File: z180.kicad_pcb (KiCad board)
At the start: 2 copper layers, 89.7 x 64.8 mm, 69 parts, among them J1 SERIAL_IO, J2 USB_POWER, J3 zdbus, J4 zabus, J5 zcbus, J6 USB_DATA, J7 POWER_IN, J8 Conn_01x08, J9 MEM_ADDR, SW1 SW_Push, U1 74LS138, U2 28C256, U3 AS6C1008-55PCN, U4 74LS138, U5 DS1813, U8 74LS05, Y1 Crystal

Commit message: layout mostly complete
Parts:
- removed C14, C17, C7, C8: 0.1µF, Capacitor_SMD:C_1206_3216Metric_Pad1.42x1.75mm_HandSolder
- removed D1, D2, D4, D5, D6, D7: LED, LED_SMD:LED_1206_3216Metric_Pad1.42x1.75mm_HandSolder
- removed J5: zcbus, Connector_IDC:IDC-Header_2x08_P2.54mm_Vertical
- removed R5, R6, R7, R8: 300, Resistor_SMD:R_1206_3216Metric_Pad1.42x1.75mm_HandSolder
- removed TP5: TST_WAIT, TestPoint:TestPoint_THTPad_1.0x1.0mm_Drill0.5mm
- removed TP6: TST_HALT, TestPoint:TestPoint_THTPad_1.0x1.0mm_Drill0.5mm
- removed U8: 74LS05, Package_SO:SOIC-14_3.9x8.7mm_P1.27mm
- added J10: BUSCTRL, Connector_PinHeader_2.54mm:PinHeader_2x04_P2.54mm_Vertical, F.Cu at (48.3, 141.0)
- added JP1: SolderJumper_2_Bridged, NetTie:NetTie-2_SMD_Pad0.5mm, F.Cu at (66.0, 152.4)
- added JP2: SolderJumper_2_Bridged, NetTie:NetTie-2_SMD_Pad0.5mm, B.Cu at (72.1, 152.4)
- added MH3: MountingHole_Pad, MountingHole:MountingHole_2.2mm_M2_Pad_Via, F.Cu at (48.3, 104.1)
- added MH4: MountingHole_Pad, MountingHole:MountingHole_2.2mm_M2_Pad_Via, F.Cu at (127.0, 104.1)
- C20: value C_Small -> 0.1µF; moved to F.Cu
- J3: footprint Connector_IDC:IDC-Header_2x08_P2.54mm_Vertical -> Connector_PinHeader_2.54mm:PinHeader_2x08_P2.54mm_Vertical
- J4: value zabus -> STATUS; footprint Connector_IDC:IDC-Header_2x08_P2.54mm_Vertical -> Connector_PinHeader_2.54mm:PinHeader_1x03_P2.54mm_Vertical
- J9: footprint Connector_PinHeader_1.27mm:PinHeader_1x06_P1.27mm_Vertical -> Connector_PinHeader_2.54mm:PinHeader_1x06_P2.54mm_Vertical
- MH2: footprint MountingHole:MountingHole_2.2mm_M2_Pad_Via -> MountingHole:MountingHole_2.2mm_M2
- R1, R3: moved to F.Cu
- R2: value 300 -> 10k
- R4: value 300 -> 22R
- U2: footprint Package_DIP:DIP-28_W15.24mm_Socket -> z180:DIP-28_Piggyback_Memory_W15.24mm_Socket
- moved J6 88.7 mm to (123.4, 149.2), turned to 270 degrees
- moved J2 87.9 mm to (123.2, 143.0), turned to 90 degrees
- moved C9 84.4 mm to (126.0, 128.5), turned to 0 degrees
- moved D3 81.3 mm to (120.9, 131.6), turned to 0 degrees
- moved R3 81.2 mm to (120.9, 134.1), turned to 0 degrees
- moved J7 80.7 mm to (125.2, 134.4), turned to 90 degrees
- moved C11 71.7 mm to (113.5, 150.4), turned to 0 degrees
- moved F1 68.5 mm to (113.8, 133.9), turned to 90 degrees
- moved C10 64.7 mm to (113.5, 140.7), turned to 0 degrees
- moved R2 52.4 mm to (85.3, 141.2), turned to 0 degrees
- moved J4 44.1 mm to (50.8, 116.8), turned to 0 degrees
- moved MH1 43.1 mm to (127.0, 152.4)
- moved C19 40.7 mm to (67.8, 152.4), turned to 0 degrees
- moved U5 34.1 mm to (72.0, 147.9), turned to 0 degrees
- moved R1 33.8 mm to (68.1, 147.8), turned to 270 degrees
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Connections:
- net Net-(R10-Pad2) renamed /G1
- net Net-(R11-Pad1) renamed /~G2B
- net Net-(R9-Pad2) renamed /CE2
- C10 pad 1: /PWRIN_5V -> /REG_5V
- C10 pad 2: Earth -> /PWRIN_GND
- C11 pad 1: /PWRIN_5V -> /REG_5V
- C11 pad 2: Earth -> /PWRIN_GND
- C19 pad 1: +5V -> /REG_5V
- C19 pad 2: Earth -> /PWRIN_GND
- C9 pad 1: +5V -> /IO_5V
- D3 pad 2: +5V -> /REG_5V
- F1 pad 1: +5V -> /REG_5V
- J3 pad 10: /D5 -> /D2
- J3 pad 11: /D4 -> /D6
- J3 pad 12: /D3 -> /D7
- J3 pad 13: /D2 -> /D4
- J3 pad 14: /D1 -> /D5
- J3 pad 16: /D0 -> /D3
- J3 pad 2: +5V -> /IO_5V
- J3 pad 3: /~RD -> /A2
- J3 pad 4: /~WR -> /A1
- J3 pad 6: /A1 -> /~WR
- J3 pad 7: /A2 -> /~RD
- J3 pad 8: /D7 -> /D0
- J3 pad 9: /D6 -> /D1
- J4 pad 1: Earth -> /~HALT
- J4 pad 2: +5V -> /~M1
- J4 pad 3: /A3 -> /ST
- J7 pad 4: Earth -> /PWRIN_GND
- MH1 pad 1: Earth -> /PWRIN_GND
- R2 pad 2: Net-(D1-Pad2) -> /~EEWR
- R3 pad 2: Earth -> /PWRIN_GND
- R4 pad 1: +5V -> /REG_5V
- R4 pad 2: Net-(D2-Pad2) -> /IO_5V
- U2 pad 27: Net-(U2-Pad27) -> /~EEWR
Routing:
- net Earth: track 203.7 -> 84.5 mm, vias 26 -> 33
- net /~BUSACK: track 115.8 -> 11.7 mm, vias 2 -> 0
- net /~MREQ: track 135.5 -> 32.0 mm, vias 1 -> 0
- net +5V: track 328.3 -> 231.9 mm, vias 5 -> 4
- net /~M1: track 99.8 -> 7.54 mm, vias 1 -> 0
- net /REG_5V: track 0.00 -> 92.0 mm
- net /PWRIN_GND: track 0.00 -> 84.1 mm
- net /~RESET: track 118.9 -> 37.9 mm, vias 2 -> 1
- net /A13: track 74.2 -> 13.4 mm
- net /D2: track 111.1 -> 51.3 mm, vias 1 -> 0
- net /A10: track 80.7 -> 23.2 mm
- net /D0: track 107.0 -> 50.6 mm, vias 1 -> 0
- net /A7: track 120.7 -> 66.4 mm
- net /A12: track 78.6 -> 26.8 mm, vias 1 -> 0
- net /D1: track 107.4 -> 57.3 mm, vias 1 -> 0
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- added copper zone on B.Cu, net /PWRIN_GND
- added copper zone on F.Cu, net /PWRIN_GND
- removed copper zone on F.Cu, net +5V
- removed copper zone on F.Cu, net /USB_Vbus
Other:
- board size 89.7 x 64.8 mm -> 83.8 x 53.3 mm
- board text added: "+"
- board text added: "-"
- board text added: "1"
- board text added: "5V A1 ~WR~ D0 D2 D7 D5 D3"
- board text added: "A10 A8 A6 A4 A3 A1 ST ~INT1~ ~NMI~"
- board text added: "A9 A7 A5 GND A2 A0 ~INT2~ ~INT0~"
- board text added: "Ax2 Ax3 Ax4 Ax5 Ax6 Ax7"
- board text added: "D3 D4 D5 D6 D7 ~CE A10 ~RD A11 A9 A8 A13 ~WR CE2 A15 +5V"
- board text added: "D7 D6 D4 D5 D2 D3 D0 D1 A19 GND A18 +5V A16 A17 A14 A15 A12 A13 A11"
- board text added: "GND A2 A0 ~RD~ D1 D6 D4 ~IORQ~"
- board text added: "GND D2 D1 D0 A0 A1 A2 A3 A4 A5 A6 A7 A12 A14 A16 NC"
- board text added: "I/O"
- board text added: "I/O Address Decoder"
- board text added: "Mem Address Decoder"
- board text added: "Piggyback ROM"
- board text added: "Power"
- board text added: "ROM/RAM"
- board text added: "RXS CKS RXA1 ~RTS0~ RXA0 ~DCD0~"
- board text added: "Reset"
- board text added: "Serial I/O"
- board text added: "TXS TXA1 CKA1 ~CTS0~ TXA0 CKA0"
- board text added: "USB data"
- board text added: "Z8S180 CPU"
- board text added: "~CTS0~ TXA0 CKA0 NC ~CKA1~ RXS ~DREQ1~ ~HALT~"
- board text added: "~INT0~ ~NMI~ ~BsReq~ ~WAIT~"
- board text added: "~INT2~ ~INT1~ ~RESET~ ~BsAck~"
- board text added: "~IORQ6~ ~IORQ4~ ~IORQ2~ ~IORQ0~"
- board text added: "~IORQ7~ ~IORQ5~ ~IORQ3~ ~IORQ1~"
- board text added: "~IORQx~ (I/O Select) Addr 0x80+8x"
- board text added: "~IORQ~ ~RFSH~ E ~MREQ~ ~WR~ ~M1~ PHI ~RD~ GND GND EXTAL XTAL ~BUSACK~ ~WAIT~ ~RESET~ ~BUSREQ~"
- board text added: "~RTS0~ ~DCD0~ RXA0 TXA1 RXA1 TXS CKS TEND1"
- board text removed: "7 6 5 4 3 2"
- board text removed: "A13 A11 A9 A7 A5 A3 GND"
- board text removed: "A14 A15 A12 A10 A8 A6 A4 5V"
- board text removed: "BUS"
- board text removed: "CKS TXA1"
- board text removed: "D0 D1 D3 D5 D7 A1 ~WR~ 5V"
- board text removed: "POWER"
- board text removed: "RX"
- board text removed: "RXA0 TXA0"
- board text removed: "RXA1 CKA1"
- board text removed: "RXS TXS"
- board text removed: "ST"
- board text removed: "TX"
- board text removed: "~BUS ACK"
- board text removed: "~BUS REQ"
- board text removed: "~DCD0 CKA0"
- board text removed: "~HALT"
- board text removed: "~INT0"
- board text removed: "~INT1"
- board text removed: "~INT2"
- board text removed: "~IORQ~ D2 D4 D6 A2 A0 ~RD~ GND"
- board text removed: "~M1"
- board text removed: "~MREQ"
- board text removed: "~NMI"
- board text removed: "~RST"
- board text removed: "~RTS0 ~CTS0"
- board text removed: "~WAIT"

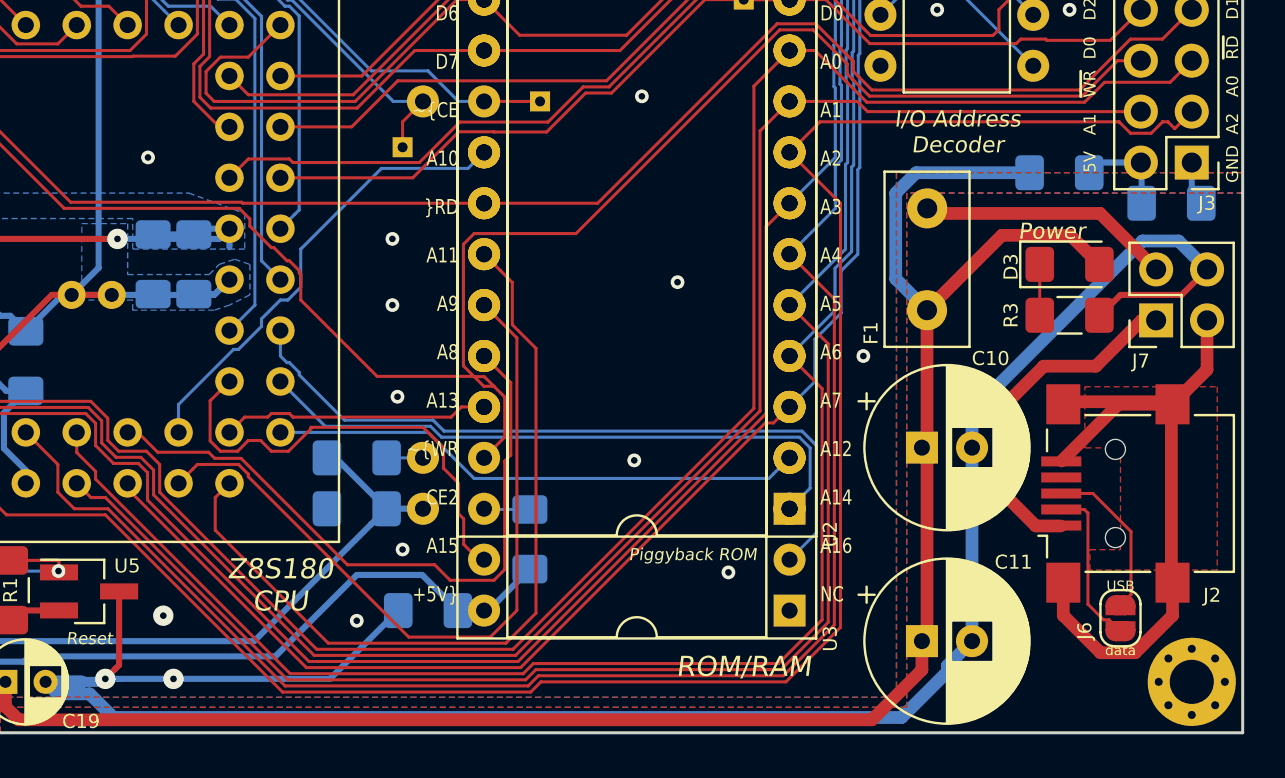
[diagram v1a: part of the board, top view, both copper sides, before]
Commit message: add logo
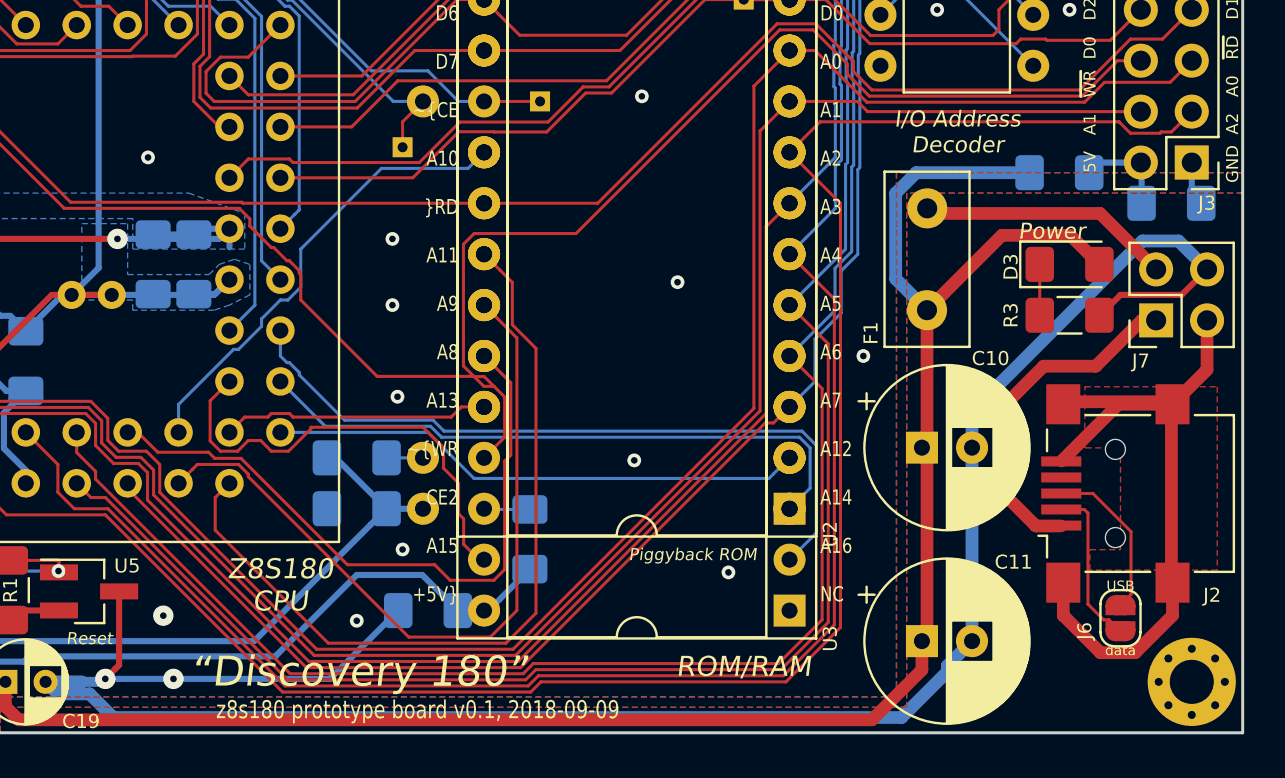
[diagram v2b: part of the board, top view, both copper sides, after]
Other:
- board text added: "USB power in"
- board text added: "i/o power"
- board text added: "power in"
- board text added: "z8s180 prototype board v0.1, 2018-09-09"
- board text added: "“Discovery 180”"

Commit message: final for v0.1
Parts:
- removed R1: [1k], Resistor_SMD:R_1206_3216Metric_Pad1.42x1.75mm_HandSolder
- added RN1: 10k x4, Resistor_SMD:R_Array_Convex_4x1206, B.Cu at (56.4, 51.8)
- added RN2: 10k x4, Resistor_SMD:R_Array_Convex_4x1206, B.Cu at (59.3, 63.0)
- added bird1: bird_logo, z180:bird, F.Cu at (70.6, 67.1)
- added bird1: SYM_Flash_Small, z180:bird, B.Cu at (97.3, 66.8)
- added discovery1: discovery_logo, z180:discovery, B.Cu at (78.5, 68.6)
- added discovery1: SYM_Flash_Small, z180:discovery, F.Cu at (89.2, 68.6)
- added oshw1: Logo_Open_Hardware_Small, Symbol:OSHW-Symbol_6.7x6mm_SilkScreen, B.Cu at (114.3, 65.5)
- F1: value 500mA -> 650mA
- J2: value USB_POWER -> USB Micro-B 105017; footprint Connector_USB:USB_Mini-B_Lumberg_2486_01_Horizontal -> Connector_USB:USB_Micro-B_Molex-105017-0001
- MH1, MH2, MH3, MH4: value MountingHole_Pad -> M2
- R3: value 330 -> 330R
- U1, U4: value 74LS138 -> 74HCT138
- moved J6 90.8 mm to (115.3, 58.8)
- moved C13 84.1 mm to (55.1, 46.0)
- moved CPU1 84.1 mm to (49.5, 46.0)
- moved J7 84.1 mm to (118.6, 50.5)
- moved TP1 84.1 mm to (54.1, 48.3)
- moved C10 84.1 mm to (106.9, 56.9)
- moved C15 84.1 mm to (97.0, 24.9)
- moved C19 84.1 mm to (61.2, 68.6)
- moved C6 84.1 mm to (78.7, 59.9)
- moved F1 84.1 mm to (107.2, 50.0)
- moved J3 84.1 mm to (120.4, 42.7)
- moved JP1 84.1 mm to (59.4, 68.6)
- moved JP2 84.1 mm to (65.5, 68.6)
- moved MH1 84.1 mm to (120.4, 68.6)
- moved MH2 84.1 mm to (41.7, 68.6)
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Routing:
- net +5V: track 231.9 -> 248.5 mm, vias 4 -> 5
- net /USB_GND: track 36.2 -> 20.6 mm
- net /~NMI: track 11.0 -> 24.6 mm
- net /~RESET: track 37.9 -> 51.0 mm
- net /~INT1: track 10.4 -> 19.6 mm
- net /~WAIT: track 12.2 -> 21.0 mm
- net /~BUSREQ: track 12.7 -> 20.6 mm
- net /~INT0: track 12.9 -> 20.8 mm
- net /USB_DM: track 8.13 -> 2.87 mm
- net /USB_DP: track 8.16 -> 3.14 mm
- net /~INT2: track 14.7 -> 18.9 mm
- net /USB_Vbus: track 17.1 -> 20.6 mm
- net Earth: track 84.5 -> 86.1 mm, vias 33 -> 32
- added copper zone on F.Cu, net /USB_Vbus
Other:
- board text added: "Status"
- board text added: "Z"
- board text added: "github.com/anyahelene/z80pcb"
- board text added: "~HALT ~M1 ST"
- board text removed: "“Discovery 180”"
